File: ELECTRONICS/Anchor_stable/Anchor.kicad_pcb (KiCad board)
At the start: 4 copper layers, 40 x 75 mm, 79 parts, among them IC1 DW3210, J1 USB_C_Receptacle_USB2.0_16P, J2 Conn_01x05_Pin, J3 Conn_01x04_Pin, J4 Conn_01x05_Pin, J5 Conn_01x02_Pin, J6 Conn_01x04_Pin, J7 Conn_Coaxial, J8 Conn_Coaxial, Q1 DMG1012T, Q2 DMG1012T, Q3 DMG1012T, SW3 SW_DIP_x05, U1 BQ24075RGT, U2 NRF52840-QFAA-R7, U3 AP7370-33FDC, Y1 TXC 8Y38472012, Y2 ECS-320-8-37B-CKY-TR, Y3 ECS-.327-6-1210B-N-TR

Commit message: Add files via upload
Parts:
- removed C24: 1p, Capacitor_SMD:C_0402_1005Metric
- removed J2: Conn_01x05_Pin, Connector_PinHeader_2.54mm:PinHeader_1x05_P2.54mm_Vertical
- added J9: Conn_01x03_Pin, Connector_PinHeader_2.54mm:PinHeader_1x03_P2.54mm_Vertical, F.Cu at (50.6, 42.3)
- moved J7 12.0 mm to (22.4, 27.5), turned to 180 degrees
- moved J8 12.0 mm to (42.4, 27.5), turned to 0 degrees
- moved R19 8.56 mm to (22.4, 56.9), turned to 90 degrees
- moved C12 2.05 mm to (34.0, 42.5), turned to -90 degrees
- moved C25 1.09 mm to (25.8, 36.5)
- moved C26 1.09 mm to (28.3, 33.7)
- moved Y1 1.09 mm to (26.4, 34.7)
- moved J4 0.05 mm to (50.6, 58.6)
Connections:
- IC1 pad 2: /DW_GPIO6 -> GNDREF
- IC1 pad 5: /DW_GPIO5 -> GNDREF
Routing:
- net /DW_RF2: track 19.7 -> 0.00 mm
- net /DW_RF1: track 19.7 -> 0.00 mm
- net /DW_GPIO6: track 17.1 -> 0.00 mm
- net /DW_GPIO5: track 16.5 -> 0.00 mm
- net GNDREF: track 42.3 -> 53.2 mm, vias 42 -> 69
- net +3V3: track 46.3 -> 49.3 mm, vias 34 -> 36
- net Net-(IC1-RF2): track 1.93 -> 0.00 mm
- net /DW_GPIO7: track 17.6 -> 15.8 mm
- net Net-(IC1-RF1): track 1.85 -> 0.43 mm
- net /XTO: track 4.21 -> 5.56 mm
- net /XTI: track 3.76 -> 4.97 mm
- net /TXLED: track 17.3 -> 16.1 mm
- net /MODE_SEL: track 30.2 -> 29.1 mm
- net /DW_GPIO0: track 16.2 -> 17.0 mm
- added copper zone on F.Cu, net GNDREF
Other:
- board size 40 x 75 mm -> 40 x 65 mm
- board text added: "3V3"
- board text added: "GND"
- board text added: "P0.10/NFC1"
- board text added: "P0.10/NFC2"
- board text added: "P0.28"
- board text added: "P0.29"
- board text added: "P0.30"
- board text added: "P0.31"
- board text added: "SWDCLK"
- board text added: "SWDIO"
- board text added: "TRACE0"
- board text added: "TRACE1"
- board text added: "TRACE2"
- board text added: "TRACE3"
- board text added: "TRACECLK"

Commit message: add reset button to anchor, polish later
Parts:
- added SW1: reset, MyFootprintLibrary:SW-SMD_L3.9-W3.0-P4.45, F.Cu at (41.8, 55.6)
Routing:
- net Net-(U2-P0.18/RESET/QSPI/CSN): track 1.24 -> 9.51 mm, vias 1 -> 2
- net GNDREF: track 53.2 -> 54.7 mm, vias 69 -> 70

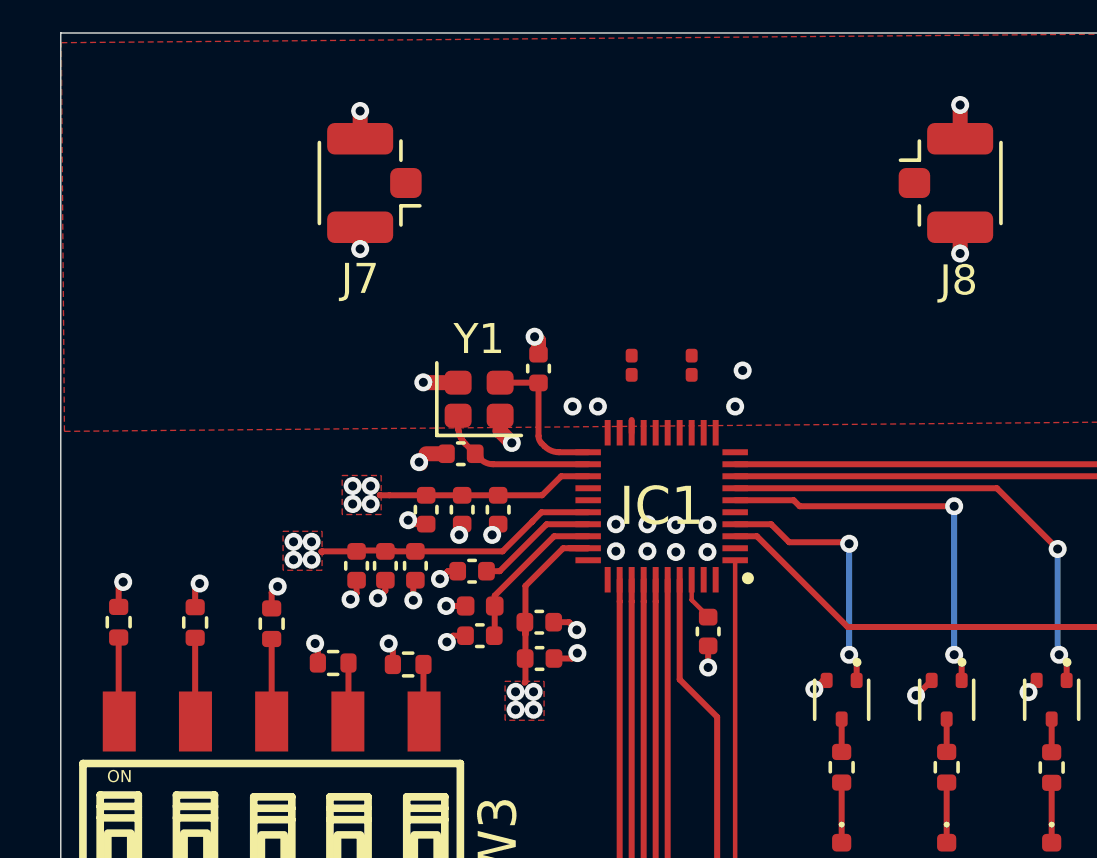
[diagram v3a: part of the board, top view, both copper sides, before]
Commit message: changed power plane, do gnd stitching soon
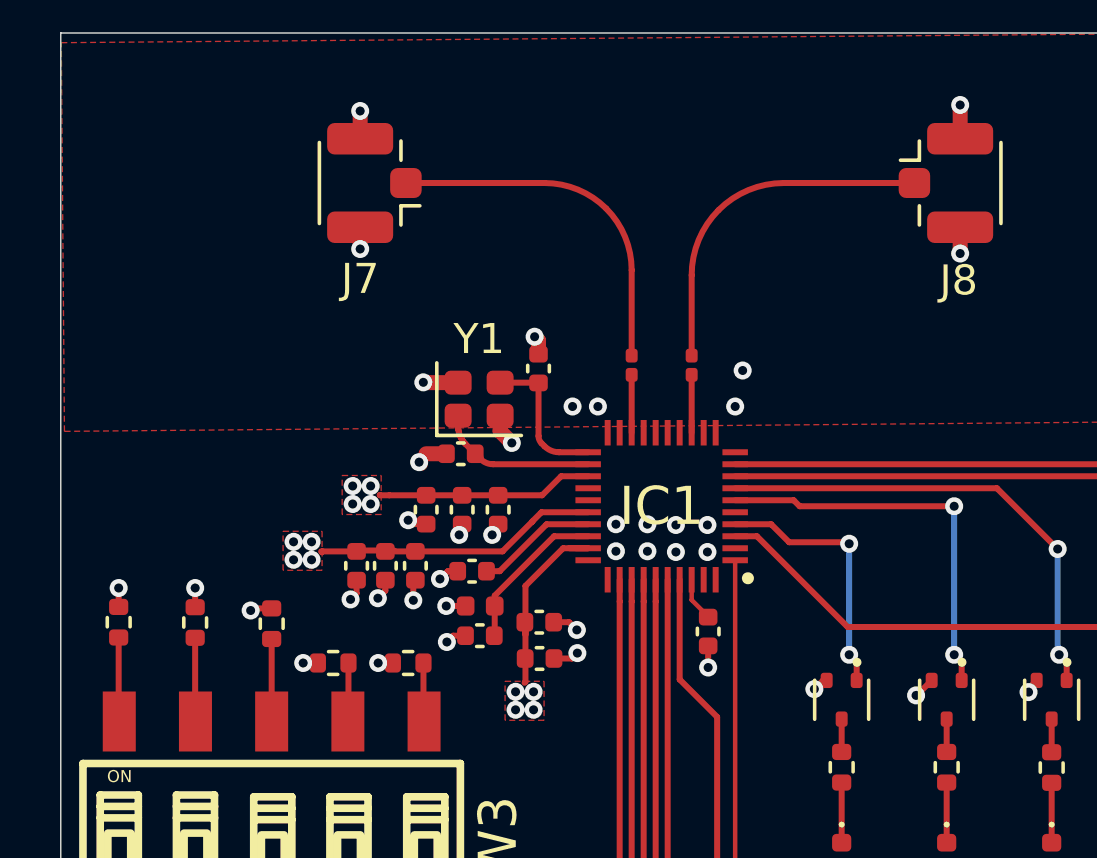
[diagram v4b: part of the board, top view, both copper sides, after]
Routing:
- net /DW_RF1: track 0.00 -> 12.0 mm
- net /DW_RF2: track 0.00 -> 11.8 mm
- net Net-(IC1-RF2): track 0.00 -> 1.93 mm
- net Net-(IC1-RF1): track 0.43 -> 1.93 mm
- net +3V3: track 49.3 -> 48.2 mm
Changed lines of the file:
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@@
 	(footprint "Resistor_SMD:R_0402_1005Metric"
 		(layer "F.Cu")
-		(at 24 43.55 180)
+		(at 24 43.5 180)
 		(descr "Resistor SMD 0402 (1005 Metric), square (rectangular) end terminal, IPC-7351 nominal, (Body size source: IPC-SM-782 page 72, https://www.pcb-3d.com/wordpress/wp-content/uploads/ipc-sm-782a_amendment_1_and_2.pdf)")
 		(tags "resistor")
@@
 	)
 	(segment
+		(start 20.5 43.5)
+		(end 20.99 43.5)
+		(width 0.2)
+		(layer "F.Cu")
+		(net "+3V3")
+	)
+	(segment
 		(start 41.95 50.46)
 		(end 41.95 50.8)
@@
 	)
 	(segment
-		(start 19.45 41.15)
-		(end 19.65 40.95)
-		(width 0.2)
-		(layer "F.Cu")
-		(net "+3V3")
-	)
-	(segment
 		(start 27.12 38.03)
 		(end 27 37.91)
@@
 	)
 	(segment
-		(start 21.14 39.78)
-		(end 22.28 39.78)
+		(start 18.75 41.75)
+		(end 18.82 41.68)
 		(width 0.2)
 		(layer "F.Cu")
@@
 	)
 	(segment
-		(start 37.02 60.325)
-		(end 37.02 60.455)
+		(start 21.14 39.78)
+		(end 22.28 39.78)
 		(width 0.2)
 		(layer "F.Cu")
@@
 	)
 	(segment
-		(start 23.49 43.55)
-		(end 23.49 42.99)
+		(start 37.02 60.325)
+		(end 37.02 60.455)
 		(width 0.2)
 		(layer "F.Cu")
@@
 	)
 	(segment
-		(start 20.99 43.5)
-		(end 20.99 42.94)
-		(width 0.2)
-		(layer "F.Cu")
-		(net "+3V3")
-	)
-	(segment
 		(start 29.165 39.675)
 		(end 27.91 40.93)
@@
 	)
 	(segment
-		(start 20.99 42.94)
-		(end 20.9 42.85)
-		(width 0.2)
-		(layer "F.Cu")
-		(net "+3V3")
-	)
-	(segment
 		(start 24.24 39.78)
 		(end 23.24 39.78)
@@
 	)
 	(segment
-		(start 19.45 41.68)
-		(end 19.45 41.15)
+		(start 14.35 41)
+		(end 14.35 41.63)
 		(width 0.2)
 		(layer "F.Cu")
@@
 	(segment
 		(start 16.9 41)
-		(end 17.05 40.85)
+		(end 16.9 41.64)
 		(width 0.2)
 		(layer "F.Cu")
@@
 	)
 	(segment
-		(start 33.0746 58.3004)
-		(end 33.0746 60.274202)
+		(start 18.82 41.68)
+		(end 19.45 41.68)
 		(width 0.2)
 		(layer "F.Cu")
@@
 	)
 	(segment
-		(start 24.6 37.91)
-		(end 25.8 37.91)
+		(start 33.0746 58.3004)
+		(end 33.0746 60.274202)
 		(width 0.2)
 		(layer "F.Cu")
@@
 	)
 	(segment
-		(start 23.49 42.99)
-		(end 23.35 42.85)
+		(start 24.6 37.91)
+		(end 25.8 37.91)
 		(width 0.2)
 		(layer "F.Cu")
@@
 	)
 	(segment
-		(start 14.35 41.63)
-		(end 14.35 40.95)
-		(width 0.2)
-		(layer "F.Cu")
-		(net "+3V3")
-	)
-	(segment
 		(start 35.83 67.07)
 		(end 35.8 67.1)
@@
 	)
 	(segment
-		(start 14.35 40.95)
-		(end 14.5 40.8)
+		(start 23 43.5)
+		(end 23.49 43.5)
 		(width 0.2)
 		(layer "F.Cu")
@@
 	)
 	(segment
-		(start 16.9 41.64)
-		(end 16.9 41)
-		(width 0.2)
-		(layer "F.Cu")
-		(net "+3V3")
-	)
-	(segment
 		(start 24.24 39.78)
 		(end 24.28 39.74)
@@
 	)
 	(via
-		(at 23.35 42.85)
+		(at 23 43.5)
 		(size 0.6)
 		(drill 0.3)
@@
 	)
 	(via
-		(at 14.5 40.8)
+		(at 14.35 41)
 		(size 0.6)
 		(drill 0.3)
@@
 	)
 	(via
-		(at 19.65 40.95)
+		(at 18.75 41.75)
 		(size 0.6)
 		(drill 0.3)
@@
 	)
 	(via
-		(at 20.9 42.85)
+		(at 20.5 43.5)
 		(size 0.6)
 		(drill 0.3)
@@
 	)
 	(via
-		(at 17.05 40.85)
+		(at 16.9 41)
 		(size 0.6)
 		(drill 0.3)
@@
 	)
 	(segment
+		(start 36.522792 27.5)
+		(end 40.875 27.5)
+		(width 0.2)
+		(layer "F.Cu")
+		(net "/DW_RF2")
+	)
+	(segment
+		(start 33.45 30.572792)
+		(end 33.45 33.255)
+		(width 0.2)
+		(layer "F.Cu")
+		(net "/DW_RF2")
+	)
+	(arc
+		(start 36.522792 27.5)
+		(mid 35.346885 27.733902)
+		(end 34.35 28.4)
+		(width 0.2)
+		(layer "F.Cu")
+		(net "/DW_RF2")
+	)
+	(arc
+		(start 34.35 28.4)
+		(mid 33.683902 29.396885)
+		(end 33.45 30.572792)
+		(width 0.2)
+		(layer "F.Cu")
+		(net "/DW_RF2")
+	)
+	(segment
+		(start 33.45 33.895)
+		(end 33.45 35.825)
+		(width 0.2)
+		(layer "F.Cu")
+		(net "Net-(IC1-RF2)")
+	)
+	(segment
 		(start 26.45 54.46)
 		(end 26.44 54.45)
@@
 	)
 	(segment
-		(start 31.45 35.825)
-		(end 31.45 35.4)
+		(start 31.45 33.895)
+		(end 31.45 35.825)
 		(width 0.2)
 		(layer "F.Cu")
@@
 	)
 	(segment
+		(start 31.45 30.402081)
+		(end 31.45 33.255)
+		(width 0.2)
+		(layer "F.Cu")
+		(net "/DW_RF1")
+	)
+	(segment
+		(start 28.547918 27.5)
+		(end 23.925 27.5)
+		(width 0.2)
+		(layer "F.Cu")
+		(net "/DW_RF1")
+	)
+	(arc
+		(start 30.6 28.35)
+		(mid 31.229092 29.291502)
+		(end 31.45 30.402081)
+		(width 0.2)
+		(layer "F.Cu")
+		(net "/DW_RF1")
+	)
+	(arc
+		(start 30.6 28.35)
+		(mid 29.658496 27.720907)
+		(end 28.547918 27.5)
+		(width 0.2)
+		(layer "F.Cu")
+		(net "/DW_RF1")
+	)
+	(segment
